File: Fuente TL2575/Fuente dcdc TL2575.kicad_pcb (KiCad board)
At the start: 2 copper layers, 53.3 x 35.6 mm, 20 parts, among them U1 TL2575

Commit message: Terminada Fuente TL2575, y controlador
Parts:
- removed the REF** at (138.2, 48.8)
- removed the REF** at (141.7, 48.8)
- removed the REF** at (145.3, 48.8)
- removed the REF** at (132.1, 48.8)
- added C5: 100uF, Capacitors_ThroughHole:C_Radial_D6.3_L11.2_P2.5, F.Cu at (137.2, 67.9)
- added D2: D, Diodes_ThroughHole:Diode_DO-41_SOD81_Horizontal_RM10, B.Cu at (119.4, 68.6)
- added D3: D, Diodes_ThroughHole:Diode_DO-41_SOD81_Horizontal_RM10, B.Cu at (119.4, 62.2)
- added REF**: 1pin, Connect:1pin, F.Cu at (145.4, 48.3)
- added REF**: 1pin, Connect:1pin, F.Cu at (147.3, 48.3)
- added REF**: 1pin, Connect:1pin, F.Cu at (143.5, 48.3)
- added REF**: 1pin, Connect:1pin, F.Cu at (141.6, 48.3)
- D1: moved to B.Cu
- Vin1: value CONN_01X02 -> CONN_01X03; footprint Sockets_WAGO734:WAGO_734_2pin_Straight_RuggedPads -> Connect:bornier3
- Vout1: footprint Sockets_WAGO734:WAGO_734_2pin_Straight_RuggedPads -> Connect:bornier2
- moved R2 21.1 mm to (121.3, 40.6), turned to 0 degrees
- moved C4 8.33 mm to (142.2, 60.7), turned to 270 degrees
- moved D1 5.59 mm to (130.8, 53.3)
- moved Vout1 5.46 mm to (148.0, 62.9)
- moved C2 5.08 mm to (125.7, 59.7), turned to 0 degrees
- moved U1 3.81 mm to (116.8, 52.1)
- moved C1 2.84 mm to (119.4, 67.3), turned to 90 degrees
- moved RV1 2.54 mm to (108.0, 44.5)
- moved R1 2.29 mm to (121.3, 44.5)
- moved Vin1 1.42 mm to (109.2, 65.4), turned to 90 degrees
- moved L1 1.14 mm to (139.7, 48.3)
- moved C3 0.64 mm to (137.2, 60.3)
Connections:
- Vin1 pad 1: Net-(C1-Pad1) -> Net-(D2-Pad1)
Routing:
- net Net-(R2-Pad1): track 4.45 -> 11.6 mm
- net Net-(D2-Pad1): track 0.00 -> 5.87 mm
- net Net-(D3-Pad1): track 0.00 -> 5.87 mm
- net Net-(R1-Pad2): track 7.40 -> 3.17 mm
- net Net-(RV1-Pad2): track 5.08 -> 3.81 mm
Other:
- board size 53.3 x 35.6 mm -> 55.9 x 38.1 mm

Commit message: Para imprimir, fuente TL2575 y Controlador
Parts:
- moved D3 12.5 mm to (108.6, 55.9), turned to 270 degrees
- moved D2 11.4 mm to (108.6, 64.8)
- moved Vin1 11.1 mm to (103.5, 55.9)
- moved C2 4.88 mm to (128.8, 63.5)
- moved C1 4.07 mm to (122.6, 64.8)
- moved R1 3.17 mm to (124.5, 44.5)
- moved R2 3.17 mm to (124.5, 40.6)
- moved RV1 3.17 mm to (111.1, 44.5)
- moved U1 3.17 mm to (120.0, 52.1)
- moved D1 1.27 mm to (132.1, 53.3)
- moved Vout1 0.64 mm to (148.0, 62.2)
- moved C4 0.60 mm to (142.2, 60.1)
- moved C3 0.25 mm to (137.4, 60.3)
- moved C5 0.25 mm to (137.4, 67.9)
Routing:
- net (no net): track 0.00 -> 53.3 mm
- net Net-(C1-Pad1): track 0.00 -> 8.12 mm
- net Net-(D2-Pad1): track 5.87 -> 3.81 mm
- net Net-(D3-Pad1): track 5.87 -> 5.08 mm

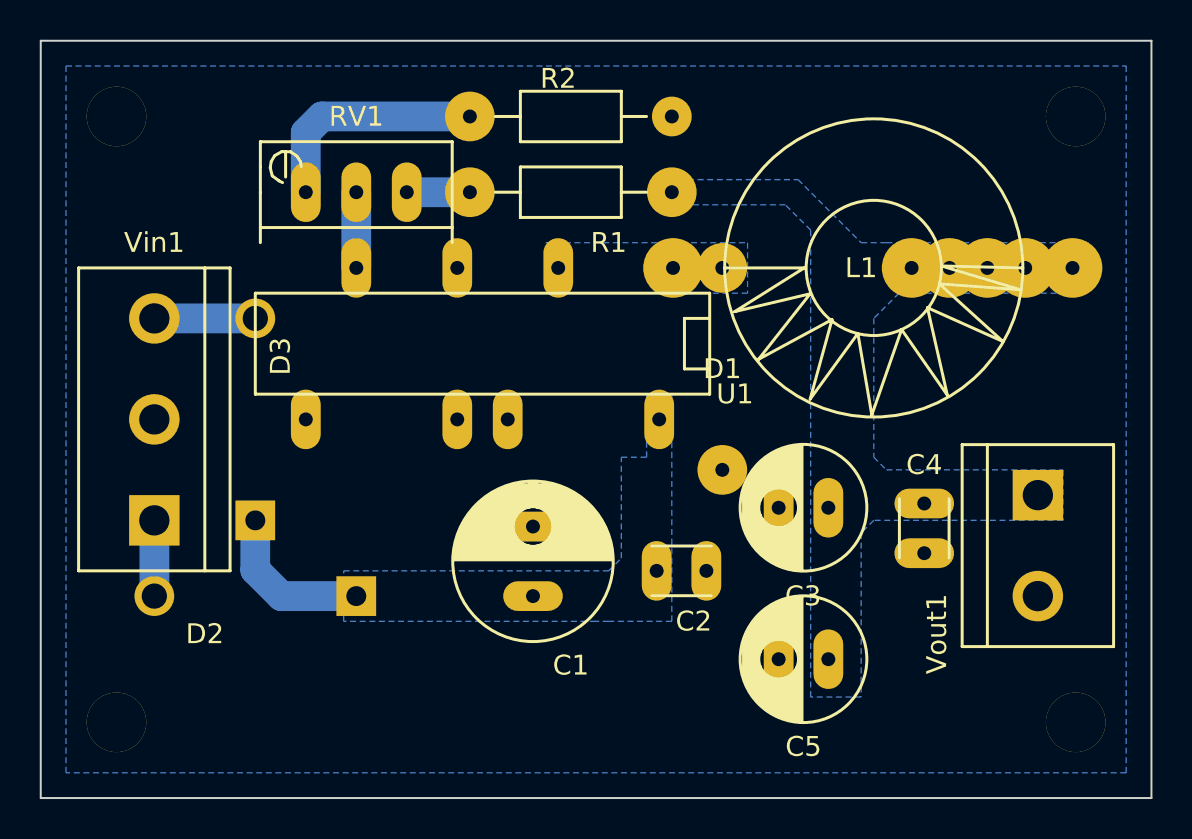
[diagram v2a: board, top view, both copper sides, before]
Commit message: Se realizó la segunda versión de la fuente TL2575
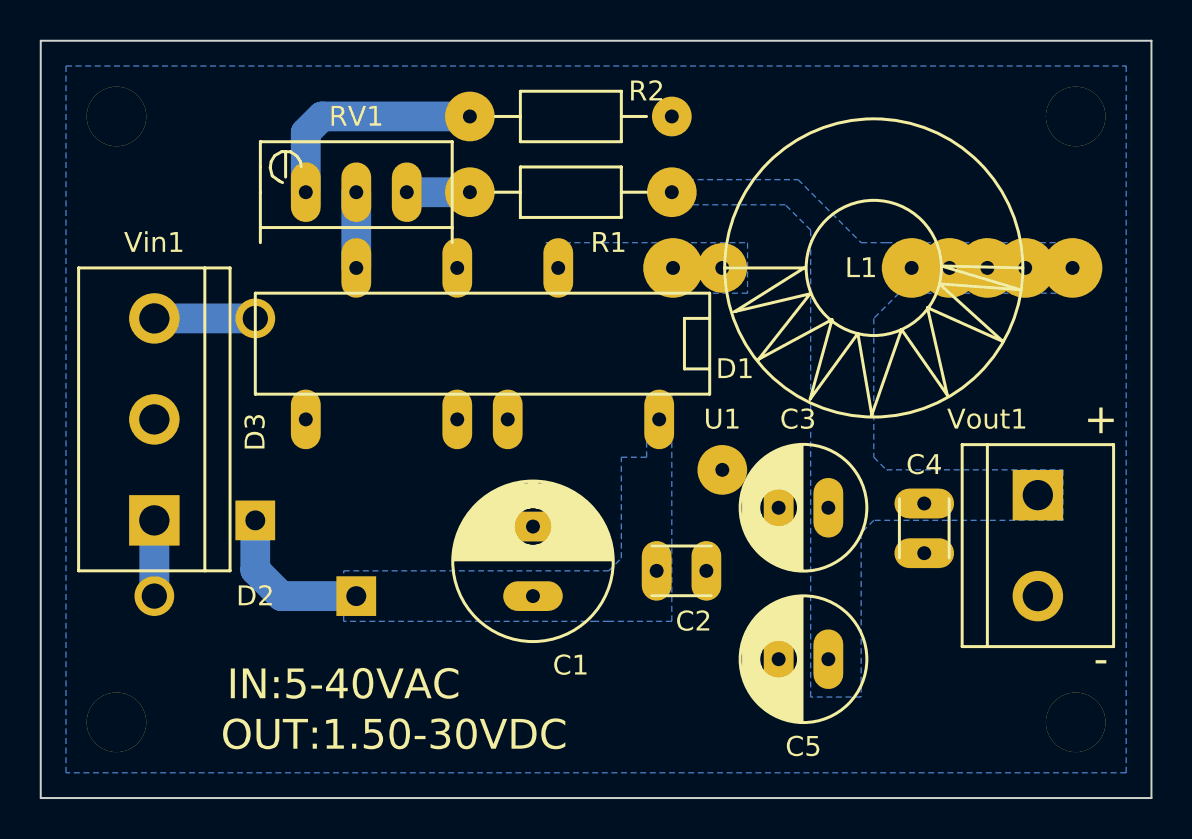
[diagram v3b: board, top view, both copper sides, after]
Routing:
- net (no net): track 53.3 -> 0.00 mm
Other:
- board text added: "+"
- board text added: "-"
- board text added: "IN:5-40VAC"
- board text added: "OUT:1.50-30VDC"
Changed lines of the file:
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@@
     (links 36)
     (no_connects 0)
-    (area -1.550001 -1.550001 158.950046 77.69626)
+    (area 85.28143 32.075 158.950046 77.69626)
     (thickness 1.6)
-    (drawings 7)
-    (tracks 11)
+    (drawings 11)
+    (tracks 10)
     (zones 0)
     (modules 23)
@@
     (descr "Diode, DO-41, SOD81, Horizontal, RM 10mm,")
     (tags "Diode, DO-41, SOD81, Horizontal, RM 10mm, 1N4007, SB140,")
-    (fp_text reference D3 (at -3.175 -1.27 270) (layer F.SilkS)
+    (fp_text reference D3 (at 0.635 0 270) (layer F.SilkS)
       (effects (font (size 1 1) (thickness 0.15)))
     )
@@
     (descr "Diode, DO-41, SOD81, Horizontal, RM 10mm,")
     (tags "Diode, DO-41, SOD81, Horizontal, RM 10mm, 1N4007, SB140,")
-    (fp_text reference D1 (at 0 0 180) (layer F.SilkS)
+    (fp_text reference D1 (at 0 0.635 180) (layer F.SilkS)
       (effects (font (size 1 1) (thickness 0.15)))
     )
@@
     (descr "16 pins DIL package, elliptical pads")
     (tags DIL)
-    (fp_text reference U1 (at -12.7 -2.54 180) (layer F.SilkS)
+    (fp_text reference U1 (at -12.065 -3.81 180) (layer F.SilkS)
       (effects (font (size 1 1) (thickness 0.15)))
     )
@@
     (descr "Resistor, Axial,  RM 10mm, 1/3W,")
     (tags "Resistor, Axial, RM 10mm, 1/3W,")
-    (fp_text reference R2 (at -0.635 -1.905) (layer F.SilkS)
+    (fp_text reference R2 (at 3.81 -1.27) (layer F.SilkS)
       (effects (font (size 1 1) (thickness 0.15)))
     )
@@
     (descr "Radial Electrolytic Capacitor, Diameter 6.3mm x Length 11.2mm, Pitch 2.5mm")
     (tags "Electrolytic Capacitor")
-    (fp_text reference C3 (at 1.27 -4.445 180) (layer F.SilkS)
+    (fp_text reference C3 (at 1.524 4.445 180) (layer F.SilkS)
       (effects (font (size 1 1) (thickness 0.15)))
     )
@@
     (descr "Diode, DO-41, SOD81, Horizontal, RM 10mm,")
     (tags "Diode, DO-41, SOD81, Horizontal, RM 10mm, 1N4007, SB140,")
-    (fp_text reference D2 (at -2.54 1.905) (layer F.SilkS)
+    (fp_text reference D2 (at 0 0) (layer F.SilkS)
       (effects (font (size 1 1) (thickness 0.15)))
     )
@@
     (descr "Bornier d'alimentation 2 pins")
     (tags DEV)
-    (fp_text reference Vout1 (at 4.445 5.08 270) (layer F.SilkS)
+    (fp_text reference Vout1 (at -6.35 2.54 360) (layer F.SilkS)
       (effects (font (size 1 1) (thickness 0.15)))
     )
@@
     )
   )
+  (gr_text IN:5-40VAC (at 113.03 69.215) (layer F.SilkS)
+    (effects (font (size 1.5 1.5) (thickness 0.3)))
+  )
+  (gr_text OUT:1.50-30VDC (at 115.57 71.755) (layer F.SilkS)
+    (effects (font (size 1.5 1.5) (thickness 0.3)))
+  )
+  (gr_text - (at 151.13 67.945) (layer F.SilkS)
+    (effects (font (size 1.5 1.5) (thickness 0.3)))
+  )
+  (gr_text + (at 151.13 55.88) (layer F.SilkS)
+    (effects (font (size 1.5 1.5) (thickness 0.3)))
+  )
   (dimension 17.78 (width 0.3) (layer Dwgs.User)
     (gr_text 17,780mm (at 91.36 46.99 270) (layer Dwgs.User)
@@
   (gr_line (start 153.67 74.93) (end 153.67 36.83) (layer Edge.Cuts) (width 0.1))
   (gr_line (start 97.79 36.83) (end 97.79 74.93) (layer Edge.Cuts) (width 0.1))
-  (segment (start 0 0) (end 53.34 0) (width 1.5) (layer Dwgs.User) (net 0))
   (segment (start 108.585 63.45949) (end 109.89551 64.77) (width 1.5) (layer B.Cu) (net 2))
-  (segment (start 108.585 60.96) (end 108.585 63.45949) (width 1.5) (layer B.Cu) (net 2))
-  (segment (start 109.89551 64.77) (end 113.665 64.77) (width 1.5) (layer B.Cu) (net 2))
-  (segment (start 116.205 44.45) (end 119.38 44.45) (width 1.5) (layer B.Cu) (net 5))
-  (segment (start 111.935 40.64) (end 119.38 40.64) (width 1.5) (layer B.Cu) (net 6))
+  (segment (start 108.585 60.96) (end 108.585 63.45949) (width 1.5) (layer B.Cu) (net 2) (status 10))
+  (segment (start 109.89551 64.77) (end 113.665 64.77) (width 1.5) (layer B.Cu) (net 2) (status 20))
+  (segment (start 116.205 44.45) (end 119.38 44.45) (width 1.5) (layer B.Cu) (net 5) (status 30))
+  (segment (start 111.935 40.64) (end 119.38 40.64) (width 1.5) (layer B.Cu) (net 6) (status 20))
   (segment (start 111.935 40.64) (end 111.125 41.45) (width 1.5) (layer B.Cu) (net 6))
-  (segment (start 111.125 41.45) (end 111.125 44.45) (width 1.5) (layer B.Cu) (net 6))
-  (segment (start 113.665 44.45) (end 113.665 48.26) (width 1.5) (layer B.Cu) (net 7))
-  (segment (start 103.505 60.96) (end 103.505 64.77) (width 1.5) (layer B.Cu) (net 8))
-  (segment (start 103.505 50.8) (end 108.585 50.8) (width 1.5) (layer B.Cu) (net 9))
+  (segment (start 111.125 41.45) (end 111.125 44.45) (width 1.5) (layer B.Cu) (net 6) (status 20))
+  (segment (start 113.665 44.45) (end 113.665 48.26) (width 1.5) (layer B.Cu) (net 7) (status 30))
+  (segment (start 103.505 60.96) (end 103.505 64.77) (width 1.5) (layer B.Cu) (net 8) (status 30))
+  (segment (start 103.505 50.8) (end 108.585 50.8) (width 1.5) (layer B.Cu) (net 9) (status 30))
   (zone (net 1) (net_name GND) (layer B.Cu) (hatch edge 0.508)
     (connect_pads yes (clearance 0.8))
